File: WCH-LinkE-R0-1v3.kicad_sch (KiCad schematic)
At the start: 38 parts, among them Q1 DMG1012UW-7, Q2 DMG1012UW-7, SW1 16V 50mA, SW2 16V 50mA, SW3 16V 50mA, U3 CH32V305FBP6

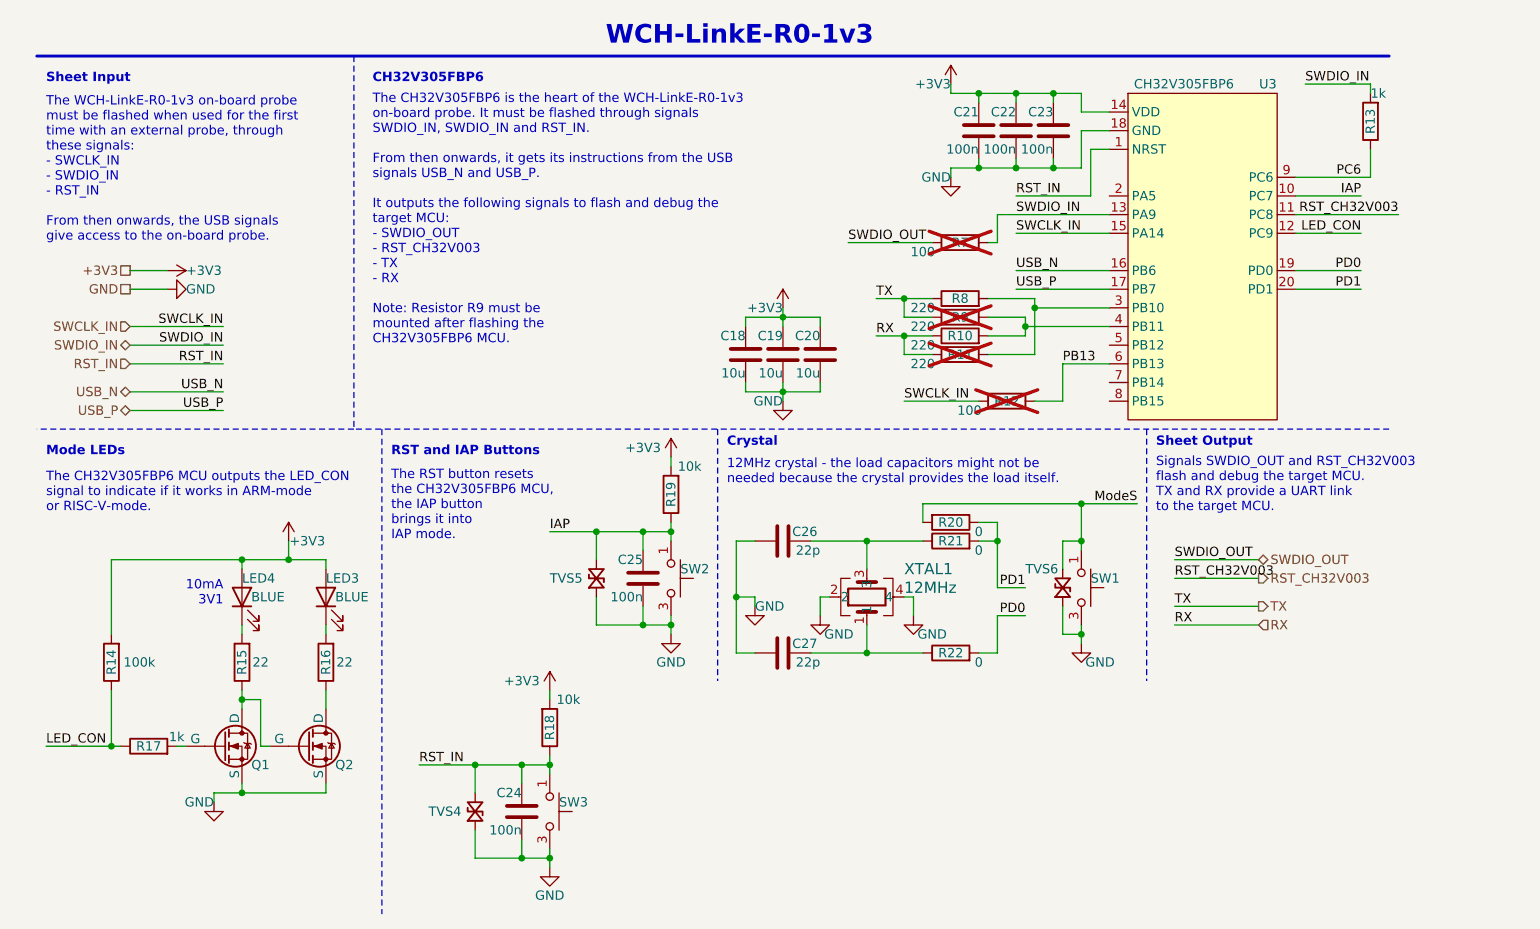
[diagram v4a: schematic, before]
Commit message: Rename net 'RST_IN' into 'RST_CH32V305'
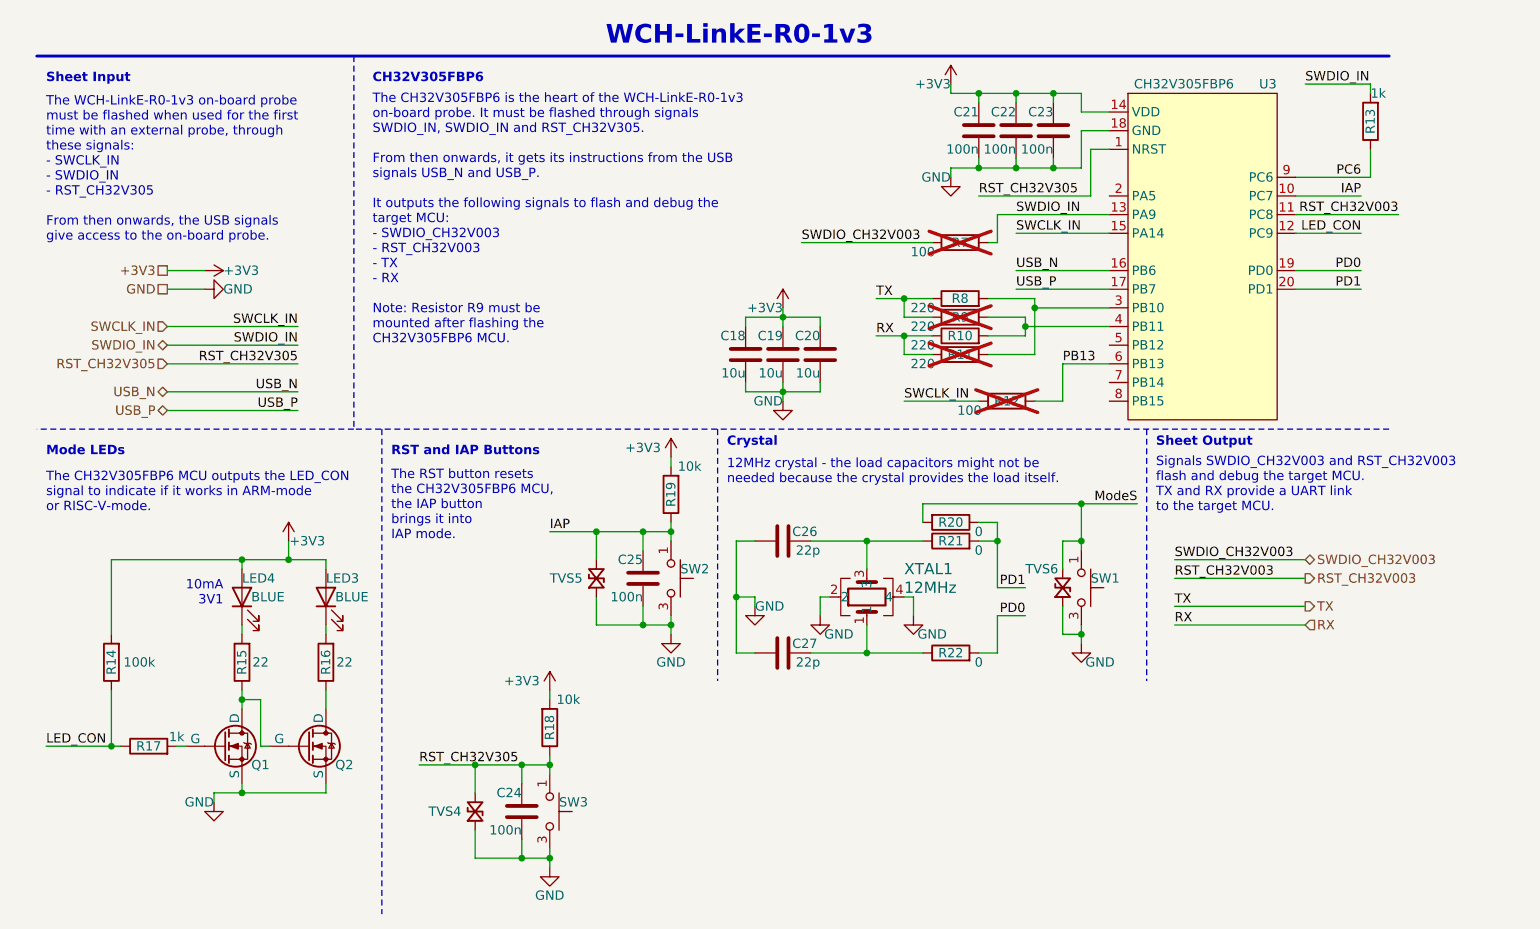
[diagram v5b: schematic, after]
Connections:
- net RST_IN renamed RST_CH32V305
- net SWDIO_OUT renamed SWDIO_CH32V003
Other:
- note added: "Signals SWDIO_CH32V003 and RST_CH32V003 flash and debug the target MCU. TX and RX provide a UART link to the target MCU."
- note added: "The CH32V305FBP6 is the heart of the WCH-LinkE-R0-1v3 on-board probe. It must be flashed through signals SWDIO_IN, SWDIO_IN and RST_CH32V305. From then onwards, it gets its instructions from the USB signals USB_N and USB_P. It outputs the following signals to flash and debug the target MCU: - SWDIO_CH32V003 - RST_CH32V003 - TX - RX Note: Resistor R9 must be mounted after flashing the CH32V305FBP6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"
- note added: "The WCH-LinkE-R0-1v3 on-board probe must be flashed when used for the first time with an external probe, through these signals: - SWCLK_IN - SWDIO_IN - RST_CH32V305 From then onwards, the USB signals give access to the on-board probe."
- note removed: "Signals SWDIO_OUT and RST_CH32V003 flash and debug the target MCU. TX and RX provide a UART link to the target MCU."
- note removed: "The CH32V305FBP6 is the heart of the WCH-LinkE-R0-1v3 on-board probe. It must be flashed through signals SWDIO_IN, SWDIO_IN and RST_IN. From then onwards, it gets its instructions from the USB signals USB_N and USB_P. It outputs the following signals to flash and debug the target MCU: - SWDIO_OUT - RST_CH32V003 - TX - RX Note: Resistor R9 must be mounted after flashing the CH32V305FBP6 MCU."
- note removed: "The WCH-LinkE-R0-1v3 on-board probe must be flashed when used for the first time with an external probe, through these signals: - SWCLK_IN - SWDIO_IN - RST_IN From then onwards, the USB signals give access to the on-board probe."

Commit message: Rename net 'SWDIO_IN' into 'SWDIO_CH32V305'
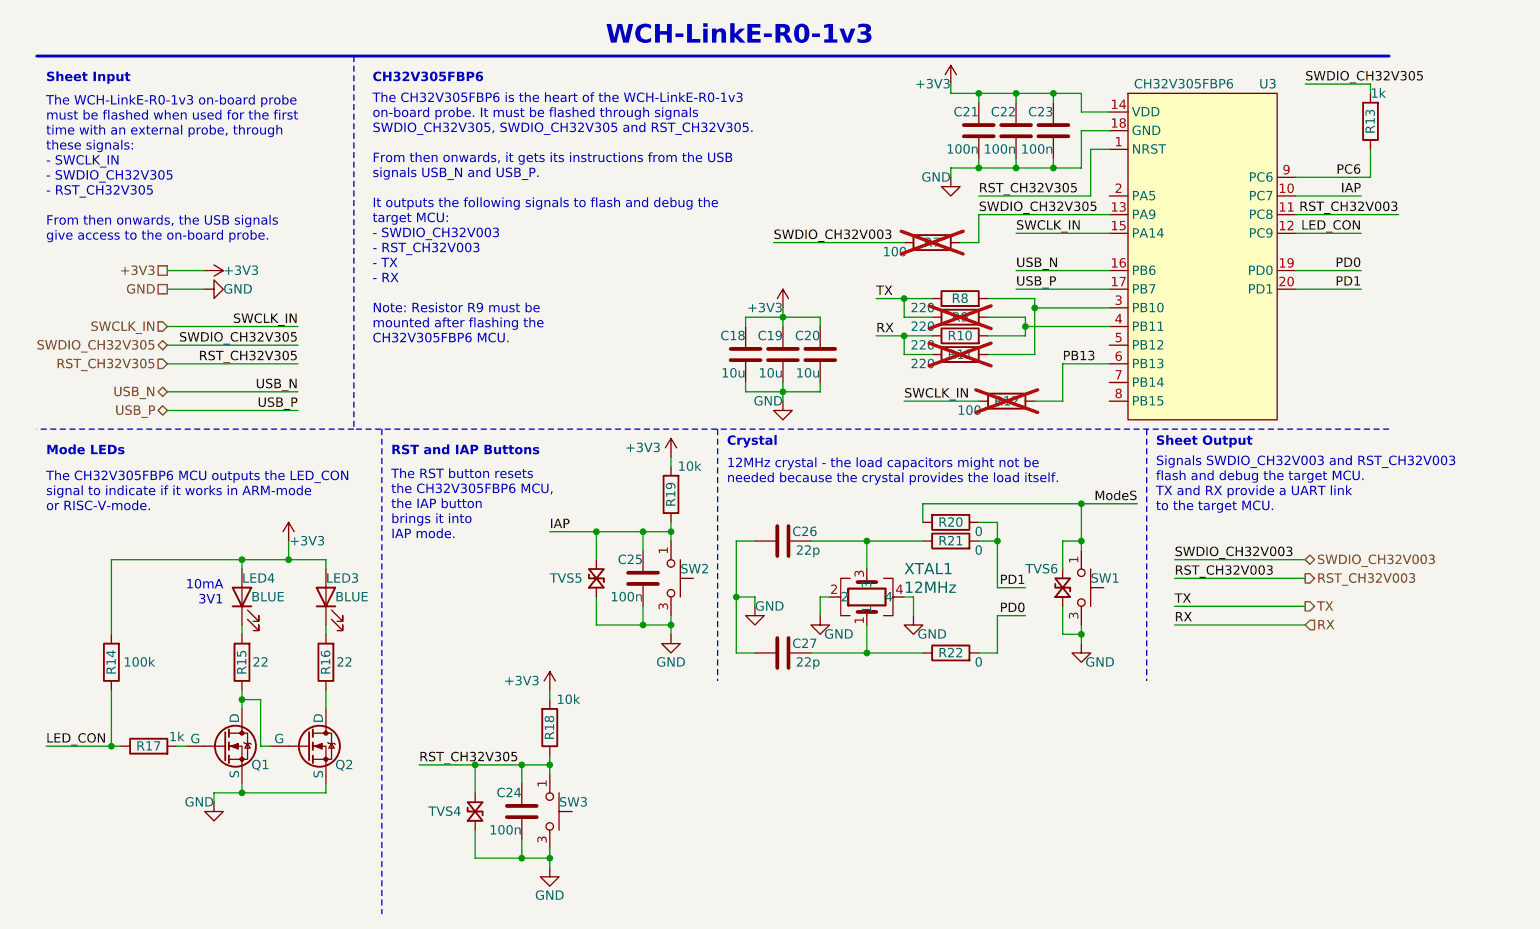
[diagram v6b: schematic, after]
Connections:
- net SWDIO_IN renamed SWDIO_CH32V305
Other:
- note added: "The CH32V305FBP6 is the heart of the WCH-LinkE-R0-1v3 on-board probe. It must be flashed through signals SWDIO_CH32V305, SWDIO_CH32V305 and RST_CH32V305. From then onwards, it gets its instructions from the USB signals USB_N and USB_P. It outputs the following signals to flash and debug the target MCU: - SWDIO_CH32V003 - RST_CH32V003 - TX - RX Note: Resistor R9 must be mounted after flashing the 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"
- note added: "The WCH-LinkE-R0-1v3 on-board probe must be flashed when used for the first time with an external probe, through these signals: - SWCLK_IN - SWDIO_CH32V305 - RST_CH32V305 From then onwards, the USB signals give access to the on-board probe."
- note removed: "The CH32V305FBP6 is the heart of the WCH-LinkE-R0-1v3 on-board probe. It must be flashed through signals SWDIO_IN, SWDIO_IN and RST_CH32V305. From then onwards, it gets its instructions from the USB signals USB_N and USB_P. It outputs the following signals to flash and debug the target MCU: - SWDIO_CH32V003 - RST_CH32V003 - TX - RX Note: Resistor R9 must be mounted after flashing the CH32V305FBP6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"
- note removed: "The WCH-LinkE-R0-1v3 on-board probe must be flashed when used for the first time with an external probe, through these signals: - SWCLK_IN - SWDIO_IN - RST_CH32V305 From then onwards, the USB signals give access to the on-board probe."
- moved on the sheet: R7
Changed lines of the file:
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@@
+    (stroke (width 0) (type default))
+  )
+  (wire (pts (xy 140.97 40.64) (xy 158.75 40.64))
     (stroke (width 0) (type default))
   )
@@
     (stroke (width 0) (type default))
   )
-  (wire (pts (xy 142.24 44.45) (xy 143.51 44.45))
+  (wire (pts (xy 138.43 44.45) (xy 140.97 44.45))
     (stroke (width 0) (type default))
   )
@@
     (stroke (width 0) (type default))
   )
-  (wire (pts (xy 116.84 44.45) (xy 134.62 44.45))
+  (wire (pts (xy 113.03 44.45) (xy 130.81 44.45))
     (stroke (width 0) (type default))
   )
   (wire (pts (xy 109.22 63.5) (xy 109.22 64.77))
-    (stroke (width 0) (type default))
-  )
-  (wire (pts (xy 143.51 40.64) (xy 158.75 40.64))
     (stroke (width 0) (type default))
   )
@@
     (stroke (width 0) (type default))
   )
-  (wire (pts (xy 143.51 44.45) (xy 143.51 40.64))
+  (wire (pts (xy 140.97 44.45) (xy 140.97 40.64))
     (stroke (width 0) (type default))
   )
@@
     (effects (font (size 1.27 1.27)) (justify left bottom))
   )
-  (text "The CH32V305FBP6 is the heart of the WCH-LinkE-R0-1v3\non-board probe. It must be flashed through signals\nSWDIO_IN, SWDIO_IN and RST_CH32V305.\n\nFrom then onwards, it gets its instructions from the USB\nsignals USB_N and USB_P.\n\nIt outputs the following signals to flash and debug the\ntarget MCU:\n- SWDIO_CH32V003\n- RST_CH32V003\n- TX\n- RX\n\nNote: Resistor R9 must be\nmounted after flashing the\nCH32V305FBP6 MCU."
+  (text "The CH32V305FBP6 is the heart of the WCH-LinkE-R0-1v3\non-board probe. It must be flashed through signals\nSWDIO_CH32V305, SWDIO_CH32V305 and RST_CH32V305.\n\nFrom then onwards, it gets its instructions from the USB\nsignals USB_N and USB_P.\n\nIt outputs the following signals to flash and debug the\ntarget MCU:\n- SWDIO_CH32V003\n- RST_CH32V003\n- TX\n- RX\n\nNote: Resistor R9 must be\nmounted after flashing the\nCH32V305FBP6 MCU."
     (at 58.42 58.42 0)
     (effects (font (size 1.27 1.27)) (justify left bottom))
   )
-  (text "The WCH-LinkE-R0-1v3 on-board probe\nmust be flashed when used for the first\ntime with an external probe, through\nthese signals:\n- SWCLK_IN\n- SWDIO_IN\n- RST_CH32V305\n\nFrom then onwards, the USB signals\ngive access to the on-board probe."
+  (text "The WCH-LinkE-R0-1v3 on-board probe\nmust be flashed when used for the first\ntime with an external probe, through\nthese signals:\n- SWCLK_IN\n- SWDIO_CH32V305\n- RST_CH32V305\n\nFrom then onwards, the USB signals\ngive access to the on-board probe."
     (at 13.97 44.45 0)
     (effects (font (size 1.27 1.27)) (justify left bottom))
@@
     (effects (font (size 1.27 1.27)) (justify left bottom))
   )
-  (label "SWDIO_CH32V003" (at 116.84 44.45 0) (fields_autoplaced)
+  (label "SWDIO_CH32V003" (at 113.03 44.45 0) (fields_autoplaced)
     (effects (font (size 1.27 1.27)) (justify left bottom))
   )
@@
     (effects (font (size 1.27 1.27)) (justify right bottom))
   )
-  (label "SWDIO_IN" (at 146.05 40.64 0) (fields_autoplaced)
+  (label "SWDIO_CH32V305" (at 140.97 40.64 0) (fields_autoplaced)
     (effects (font (size 1.27 1.27)) (justify left bottom))
   )
@@
     (effects (font (size 1.27 1.27)) (justify left bottom))
   )
-  (label "SWDIO_IN" (at 185.42 22.86 0) (fields_autoplaced)
+  (label "SWDIO_CH32V305" (at 185.42 22.86 0) (fields_autoplaced)
     (effects (font (size 1.27 1.27)) (justify left bottom))
   )
@@
     (effects (font (size 1.27 1.27)) (justify left bottom))
   )
-  (label "SWDIO_IN" (at 48.26 58.42 180) (fields_autoplaced)
+  (label "SWDIO_CH32V305" (at 48.26 58.42 180) (fields_autoplaced)
     (effects (font (size 1.27 1.27)) (justify right bottom))
   )
@@
     (effects (font (size 1.27 1.27)) (justify right))
   )
-  (hierarchical_label "SWDIO_IN" (shape bidirectional) (at 30.48 58.42 180) (fields_autoplaced)
+  (hierarchical_label "SWDIO_CH32V305" (shape bidirectional) (at 30.48 58.42 180) (fields_autoplaced)
     (effects (font (size 1.27 1.27)) (justify right))
   )
@@
     )
   )
-  (symbol (lib_id "Device:R") (at 138.43 44.45 90) (unit 1)
+  (symbol (lib_id "Device:R") (at 134.62 44.45 90) (unit 1)
     (in_bom no) (on_board yes) (dnp yes)
-    (property "Reference" "R7" (at 138.43 44.45 90)
-      (effects (font (size 1.27 1.27)))
-    )
-    (property "Value" "100" (at 133.35 45.72 90)
-      (effects (font (size 1.27 1.27)))
-    )
-    (property "Footprint" "Resistor_SMD:R_0402_1005Metric_Pad0.72x0.64mm_HandSolder" (at 138.43 46.228 90)
-      (effects (font (size 1.27 1.27)) hide)
-    )
-    (property "Datasheet" "~" (at 138.43 44.45 0)
-      (effects (font (size 1.27 1.27)) hide)
-    )
-    (property "Manufacturer" "UNI-ROYAL(Uniroyal Elec)" (at 138.43 44.45 0)
-      (effects (font (size 1.27 1.27)) hide)
-    )
-    (property "MPN" "0402WGF1000TCE" (at 138.43 44.45 90)
-      (effects (font (size 1.27 1.27)) hide)
-    )
-    (property "JLCPCB Part #" "C25076" (at 138.43 44.45 90)
-      (effects (font (size 1.27 1.27)) hide)
-    )
+    (property "Reference" "R7" (at 134.62 44.45 90)
+      (effects (font (size 1.27 1.27)))
+    )
+    (property "Value" "100" (at 129.54 45.72 90)
+      (effects (font (size 1.27 1.27)))
+    )
+    (property "Footprint" "Resistor_SMD:R_0402_1005Metric_Pad0.72x0.64mm_HandSolder" (at 134.62 46.228 90)
+      (effects (font (size 1.27 1.27)) hide)
+    )
+    (property "Datasheet" "~" (at 134.62 44.45 0)
+      (effects (font (size 1.27 1.27)) hide)
+    )
+    (property "Manufacturer" "UNI-ROYAL(Uniroyal Elec)" (at 134.62 44.45 0)
+      (effects (font (size 1.27 1.27)) hide)
+    )
+    (property "MPN" "0402WGF1000TCE" (at 134.62 44.45 90)
+      (effects (font (size 1.27 1.27)) hide)
+    )
+    (property "JLCPCB Part #" "C25076" (at 134.62 44.45 90)
+      (effects (font (size 1.27 1.27)) hide)
+    )
